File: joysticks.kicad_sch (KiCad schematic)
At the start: 43 parts, among them J1 DB9_Male_MountingHoles, J2 DB9_Male_MountingHoles

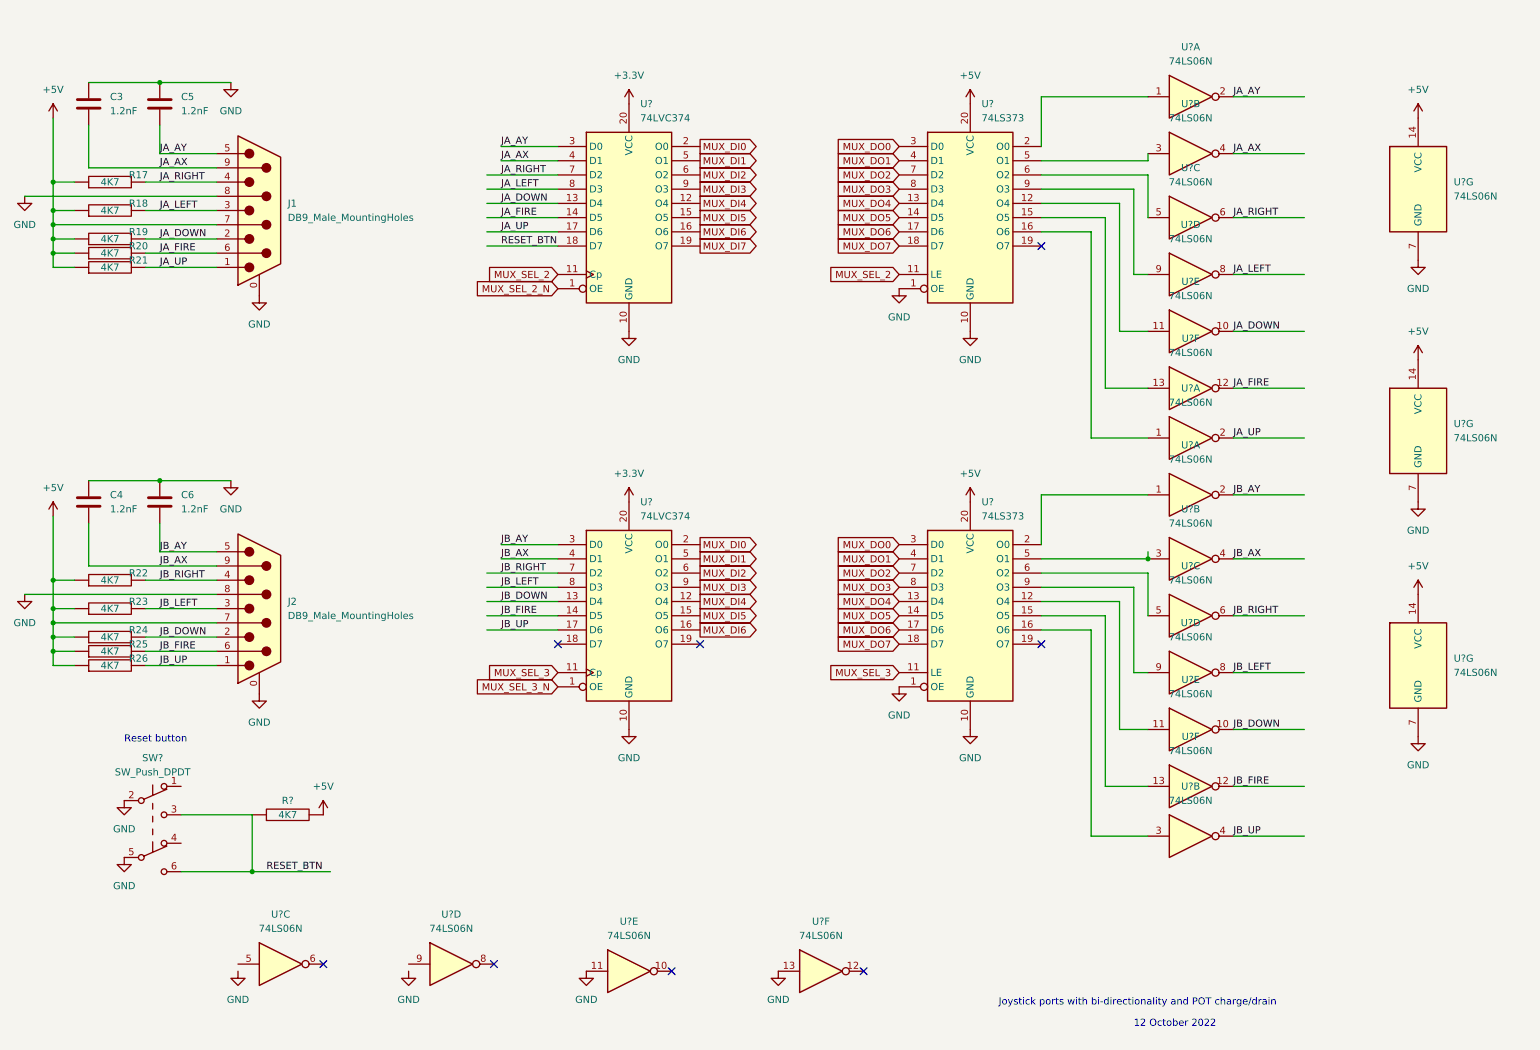
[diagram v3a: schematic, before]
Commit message: add all missing footprints
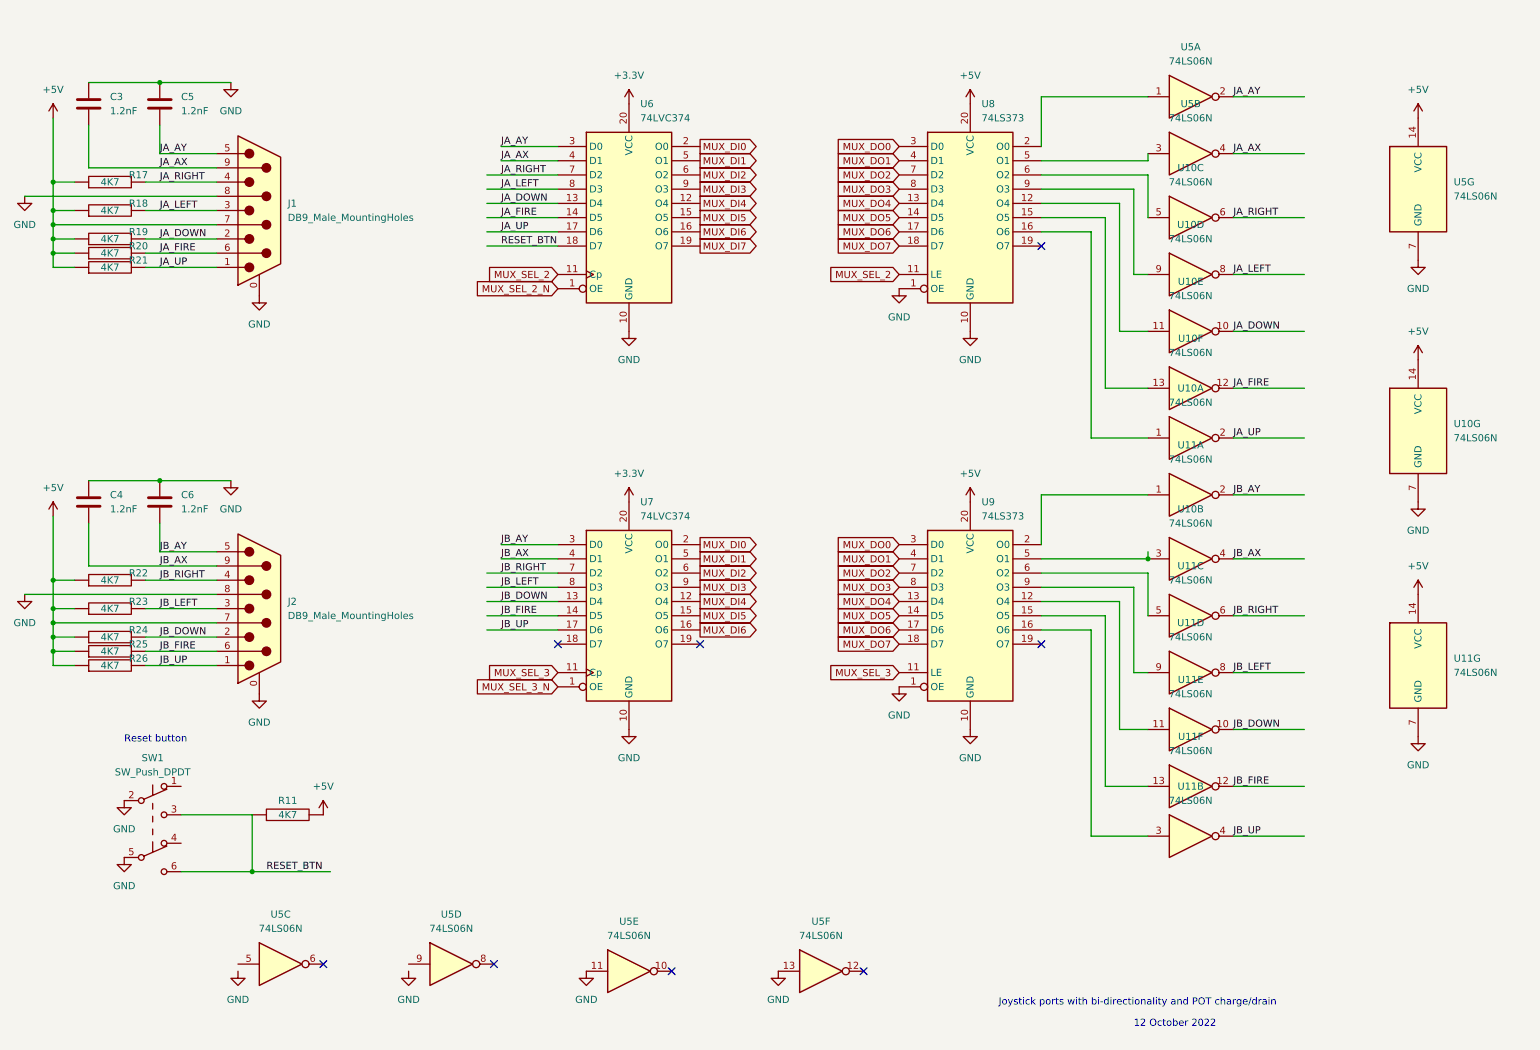
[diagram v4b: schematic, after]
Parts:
- R11: renamed from R?; footprint (none) -> Resistor_THT:R_Box_L8.4mm_W2.5mm_P5.08mm
- U10, U11, U5: renamed from U?; footprint (none) -> Package_DIP:DIP-14_W7.62mm
- gave numbers to parts that had none: 5

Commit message: add mezannine for joystick ports to de-clutter board.
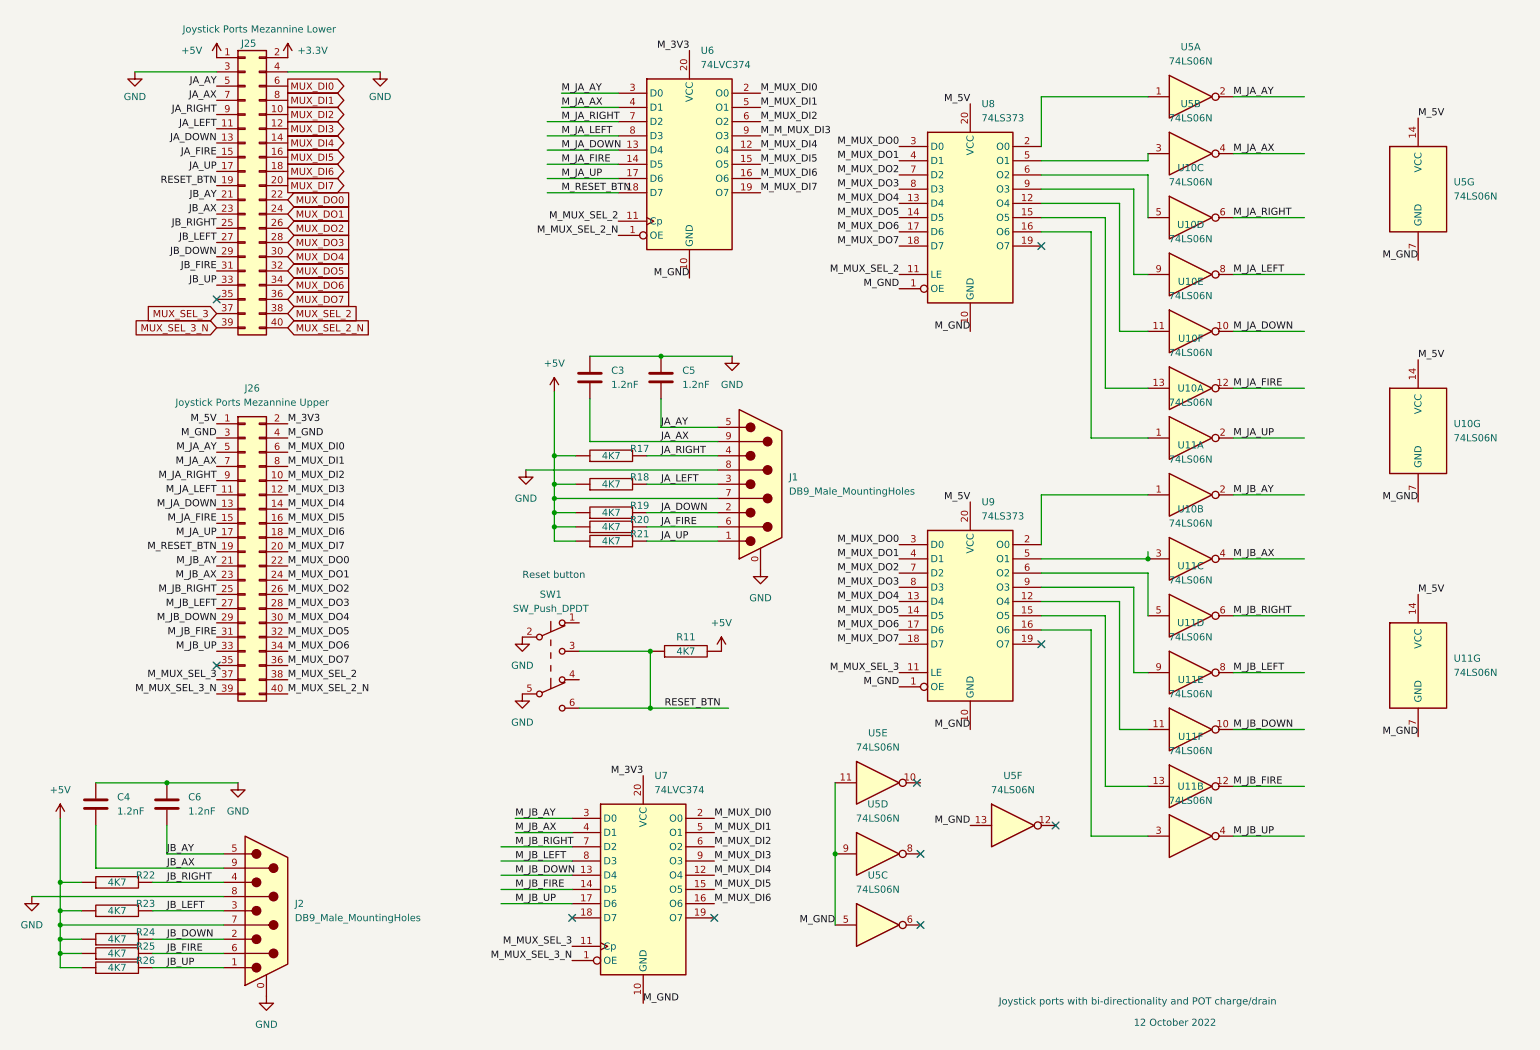
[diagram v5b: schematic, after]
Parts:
- added J25: Joystick Ports Mezannine Lower, Connector_PinHeader_2.54mm:PinHeader_2x20_P2.54mm_Vertical, symbol Connector_Generic:Conn_02x20_Odd_Even
- added J26: Joystick Ports Mezannine Upper, Connector_PinHeader_2.54mm:PinHeader_2x20_P2.54mm_Vertical, symbol Connector_Generic:Conn_02x20_Odd_Even
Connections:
- net +3V3: now also J25.2 (Pin_2); no longer U6.20 (VCC), U7.20 (VCC)
- net +5V: now also J25.1 (Pin_1); no longer U10.14 (VCC), U11.14 (VCC), U5.14 (VCC), U8.20 (VCC), U9.20 (VCC)
- net GND: now also J25.3 (Pin_3), J25.4 (Pin_4); no longer U10.7 (GND), U11.7 (GND), U5.11, U5.13, U5.7 (GND), U6.10 (GND), U7.10 (GND), U8.1 (OE), U8.10 (GND), U9.1 (OE), U9.10 (GND)
- net JA_AX: now also J25.7 (Pin_7); no longer U5.4, U6.4 (D1)
- net JA_AY: now also J25.5 (Pin_5); no longer U5.2, U6.3 (D0)
- net JA_DOWN: now also J25.13 (Pin_13); no longer U10.10, U6.13 (D4)
- net JA_FIRE: now also J25.15 (Pin_15); no longer U10.12, U6.14 (D5)
- net JA_LEFT: now also J25.11 (Pin_11); no longer U10.8, U6.8 (D3)
- net JA_RIGHT: now also J25.9 (Pin_9); no longer U10.6, U6.7 (D2)
- net JA_UP: now also J25.17 (Pin_17); no longer U10.2, U6.17 (D6)
- net JB_AX: now also J25.23 (Pin_23); no longer U10.4, U7.4 (D1)
- net JB_AY: now also J25.21 (Pin_21); no longer U11.2, U7.3 (D0)
- net JB_DOWN: now also J25.29 (Pin_29); no longer U11.10, U7.13 (D4)
- net JB_FIRE: now also J25.31 (Pin_31); no longer U11.12, U7.14 (D5)
- net JB_LEFT: now also J25.27 (Pin_27); no longer U11.8, U7.8 (D3)
- net JB_RIGHT: now also J25.25 (Pin_25); no longer U11.6, U7.7 (D2)
- net JB_UP: now also J25.33 (Pin_33); no longer U11.4, U7.17 (D6)
- net MUX_DI0: now also J25.6 (Pin_6); no longer U6.2 (O0), U7.2 (O0)
- net MUX_DI1: now also J25.8 (Pin_8); no longer U6.5 (O1), U7.5 (O1)
- net MUX_DI2: now also J25.10 (Pin_10); no longer U6.6 (O2), U7.6 (O2)
- net MUX_DI3: now also J25.12 (Pin_12); no longer U6.9 (O3), U7.9 (O3)
- net MUX_DI4: now also J25.14 (Pin_14); no longer U6.12 (O4), U7.12 (O4)
- net MUX_DI5: now also J25.16 (Pin_16); no longer U6.15 (O5), U7.15 (O5)
- net MUX_DI6: now also J25.18 (Pin_18); no longer U6.16 (O6), U7.16 (O6)
- net MUX_DI7: now also J25.20 (Pin_20); no longer U6.19 (O7)
- net MUX_DO0: now also J25.22 (Pin_22); no longer U8.3 (D0), U9.3 (D0)
- net MUX_DO1: now also J25.24 (Pin_24); no longer U8.4 (D1), U9.4 (D1)
- net MUX_DO2: now also J25.26 (Pin_26); no longer U8.7 (D2), U9.7 (D2)
- net MUX_DO3: now also J25.28 (Pin_28); no longer U8.8 (D3), U9.8 (D3)
- net MUX_DO4: now also J25.30 (Pin_30); no longer U8.13 (D4), U9.13 (D4)
- net MUX_DO5: now also J25.32 (Pin_32); no longer U8.14 (D5), U9.14 (D5)
- net MUX_DO6: now also J25.34 (Pin_34); no longer U8.17 (D6), U9.17 (D6)
- net MUX_DO7: now also J25.36 (Pin_36); no longer U8.18 (D7), U9.18 (D7)
- net MUX_SEL_2: now also J25.38 (Pin_38); no longer U6.11 (Cp), U8.11 (LE)
- net MUX_SEL_2_N: now also J25.40 (Pin_40); no longer U6.1 (OE)
- net MUX_SEL_3: now also J25.37 (Pin_37); no longer U7.11 (Cp), U9.11 (LE)
- net MUX_SEL_3_N: now also J25.39 (Pin_39); no longer U7.1 (OE)
- net RESET_BTN: now also J25.19 (Pin_19); no longer U6.18 (D7)
- net M_GND: now reaches U5.9
- net M_GND: now also U10.7 (GND), U11.7 (GND), U5.11, U5.13, U5.5, U5.7 (GND), U6.10 (GND), U7.10 (GND), U8.1 (OE), U8.10 (GND), U9.1 (OE), U9.10 (GND), J26.3 (Pin_3), J26.4 (Pin_4)
- new net M_3V3: J26.2 (Pin_2), U6.20 (VCC), U7.20 (VCC)
- new net M_5V: J26.1 (Pin_1), U10.14 (VCC), U11.14 (VCC), U5.14 (VCC), U8.20 (VCC), U9.20 (VCC)
- new net M_JA_AX: J26.7 (Pin_7), U5.4, U6.4 (D1)
- new net M_JA_AY: J26.5 (Pin_5), U5.2, U6.3 (D0)
- new net M_JA_DOWN: J26.13 (Pin_13), U10.10, U6.13 (D4)
- new net M_JA_FIRE: J26.15 (Pin_15), U10.12, U6.14 (D5)
- new net M_JA_LEFT: J26.11 (Pin_11), U10.8, U6.8 (D3)
- new net M_JA_RIGHT: J26.9 (Pin_9), U10.6, U6.7 (D2)
- new net M_JA_UP: J26.17 (Pin_17), U10.2, U6.17 (D6)
- new net M_JB_AX: J26.23 (Pin_23), U10.4, U7.4 (D1)
- new net M_JB_AY: J26.21 (Pin_21), U11.2, U7.3 (D0)
- new net M_JB_DOWN: J26.29 (Pin_29), U11.10, U7.13 (D4)
- new net M_JB_FIRE: J26.31 (Pin_31), U11.12, U7.14 (D5)
- new net M_JB_LEFT: J26.27 (Pin_27), U11.8, U7.8 (D3)
- new net M_JB_RIGHT: J26.25 (Pin_25), U11.6, U7.7 (D2)
- new net M_JB_UP: J26.33 (Pin_33), U11.4, U7.17 (D6)
- new net M_MUX_DI0: J26.6 (Pin_6), U6.2 (O0), U7.2 (O0)
- new net M_MUX_DI1: J26.8 (Pin_8), U6.5 (O1), U7.5 (O1)
- new net M_MUX_DI2: J26.10 (Pin_10), U6.6 (O2), U7.6 (O2)
- new net M_MUX_DI3: J26.12 (Pin_12), U7.9 (O3)
- new net M_MUX_DI4: J26.14 (Pin_14), U6.12 (O4), U7.12 (O4)
- new net M_MUX_DI5: J26.16 (Pin_16), U6.15 (O5), U7.15 (O5)
- new net M_MUX_DI6: J26.18 (Pin_18), U6.16 (O6), U7.16 (O6)
- new net M_MUX_DI7: J26.20 (Pin_20), U6.19 (O7)
- new net M_MUX_DO0: J26.22 (Pin_22), U8.3 (D0), U9.3 (D0)
- new net M_MUX_DO1: J26.24 (Pin_24), U8.4 (D1), U9.4 (D1)
- new net M_MUX_DO2: J26.26 (Pin_26), U8.7 (D2), U9.7 (D2)
- new net M_MUX_DO3: J26.28 (Pin_28), U8.8 (D3), U9.8 (D3)
- new net M_MUX_DO4: J26.30 (Pin_30), U8.13 (D4), U9.13 (D4)
- new net M_MUX_DO5: J26.32 (Pin_32), U8.14 (D5), U9.14 (D5)
- new net M_MUX_DO6: J26.34 (Pin_34), U8.17 (D6), U9.17 (D6)
- new net M_MUX_DO7: J26.36 (Pin_36), U8.18 (D7), U9.18 (D7)
- new net M_MUX_SEL_2: J26.38 (Pin_38), U6.11 (Cp), U8.11 (LE)
- new net M_MUX_SEL_2_N: J26.40 (Pin_40), U6.1 (OE)
- new net M_MUX_SEL_3: J26.37 (Pin_37), U7.11 (Cp), U9.11 (LE)
- new net M_MUX_SEL_3_N: J26.39 (Pin_39), U7.1 (OE)
- new net M_M_MUX_DI3: U6.9 (O3)
- new net M_RESET_BTN: J26.19 (Pin_19), U6.18 (D7)
- no-connect marks 8 -> 10
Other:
- moved on the sheet: C3, C4, C5, C6, J1, J2, R11, R17, R18, R19, R20, R21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

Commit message: start routing joystick mezzannine
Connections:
- net M_3V3 is gone; now on net +3V3: J26.2 (Pin_2), U6.20 (VCC), U7.20 (VCC)
- net M_5V is gone; now on net +5V: J26.1 (Pin_1), U10.14 (VCC), U11.14 (VCC), U5.14 (VCC), U8.20 (VCC), U9.20 (VCC)
- net M_GND is gone; now on net GND: J26.3 (Pin_3), J26.4 (Pin_4), U10.7 (GND), U11.7 (GND), U5.11, U5.13, U5.5, U5.7 (GND), U5.9, U6.10 (GND), U7.10 (GND), U8.1 (OE), U8.10 (GND), U9.1 (OE), U9.10 (GND)
- net JA_AX: now also J25.15 (Pin_15); no longer J25.7 (Pin_7)
- net JA_AY: now also J25.17 (Pin_17); no longer J25.5 (Pin_5)
- net JA_DOWN: now also J25.9 (Pin_9); no longer J25.13 (Pin_13)
- net JA_FIRE: now also J25.7 (Pin_7); no longer J25.15 (Pin_15)
- net JA_RIGHT: now also J25.13 (Pin_13); no longer J25.9 (Pin_9)
- net JA_UP: now also J25.5 (Pin_5); no longer J25.17 (Pin_17)
- net JB_AX: now also J25.31 (Pin_31); no longer J25.23 (Pin_23)
- net JB_AY: now also J25.33 (Pin_33); no longer J25.21 (Pin_21)
- net JB_DOWN: now also J25.25 (Pin_25); no longer J25.29 (Pin_29)
- net JB_FIRE: now also J25.23 (Pin_23); no longer J25.31 (Pin_31)
- net JB_RIGHT: now also J25.29 (Pin_29); no longer J25.25 (Pin_25)
- net JB_UP: now also J25.21 (Pin_21); no longer J25.33 (Pin_33)
- net M_JA_AX: now also J26.15 (Pin_15); no longer J26.7 (Pin_7)
- net M_JA_AY: now also J26.17 (Pin_17); no longer J26.5 (Pin_5)
- net M_JA_DOWN: now also J26.9 (Pin_9); no longer J26.13 (Pin_13)
- net M_JA_FIRE: now also J26.7 (Pin_7); no longer J26.15 (Pin_15)
- net M_JA_RIGHT: now also J26.13 (Pin_13); no longer J26.9 (Pin_9)
- net M_JA_UP: now also J26.5 (Pin_5); no longer J26.17 (Pin_17)
- net M_JB_AX: now also J26.31 (Pin_31); no longer J26.23 (Pin_23)
- net M_JB_AY: now also J26.33 (Pin_33); no longer J26.21 (Pin_21)
- net M_JB_DOWN: now also J26.25 (Pin_25); no longer J26.29 (Pin_29)
- net M_JB_FIRE: now also J26.23 (Pin_23); no longer J26.31 (Pin_31)
- net M_JB_RIGHT: now also J26.29 (Pin_29); no longer J26.25 (Pin_25)
- net M_JB_UP: now also J26.21 (Pin_21); no longer J26.33 (Pin_33)
- net M_MUX_DO4: now also U8.14 (D5); no longer U8.13 (D4)
- net M_MUX_DO5: now also U8.13 (D4); no longer U8.14 (D5)
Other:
- moved on the sheet: U10G, U11G, U5G
